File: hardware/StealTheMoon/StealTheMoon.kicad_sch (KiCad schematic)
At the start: 21 parts, among them J1 Motor, J2 Motor, J3 Servo, J4 Servo, J5 Conn_01x10, J6 BAT, U1 ESP32-DEVKIT-V1, U2 ROB-14450, U3 L7805CV, U4 L7805CV

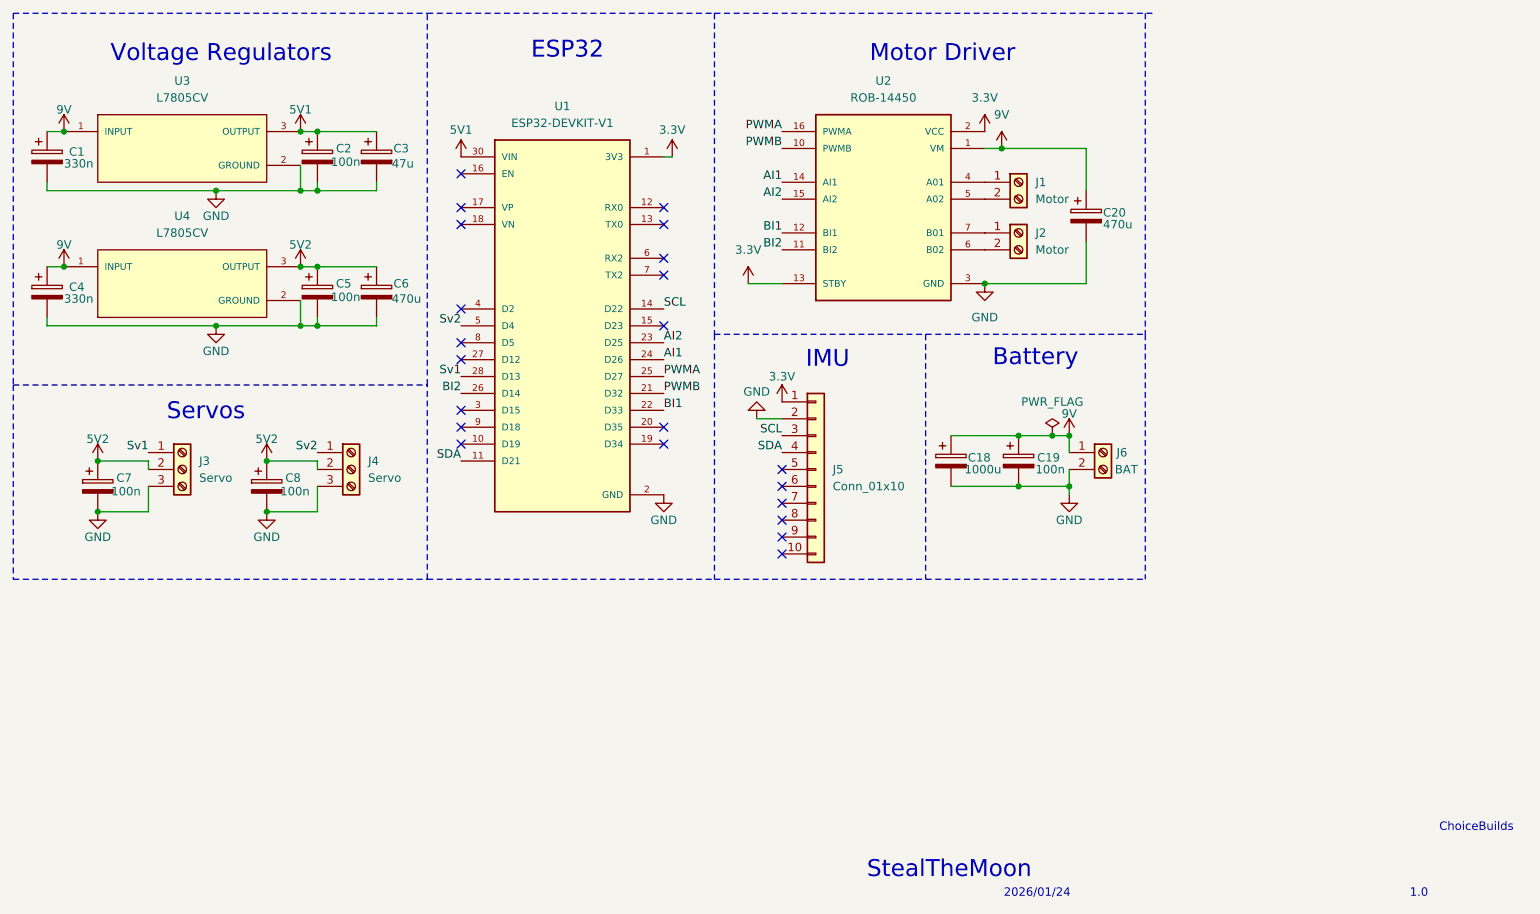
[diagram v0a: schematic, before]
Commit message: Finish layout and generate gbr files for fabrication
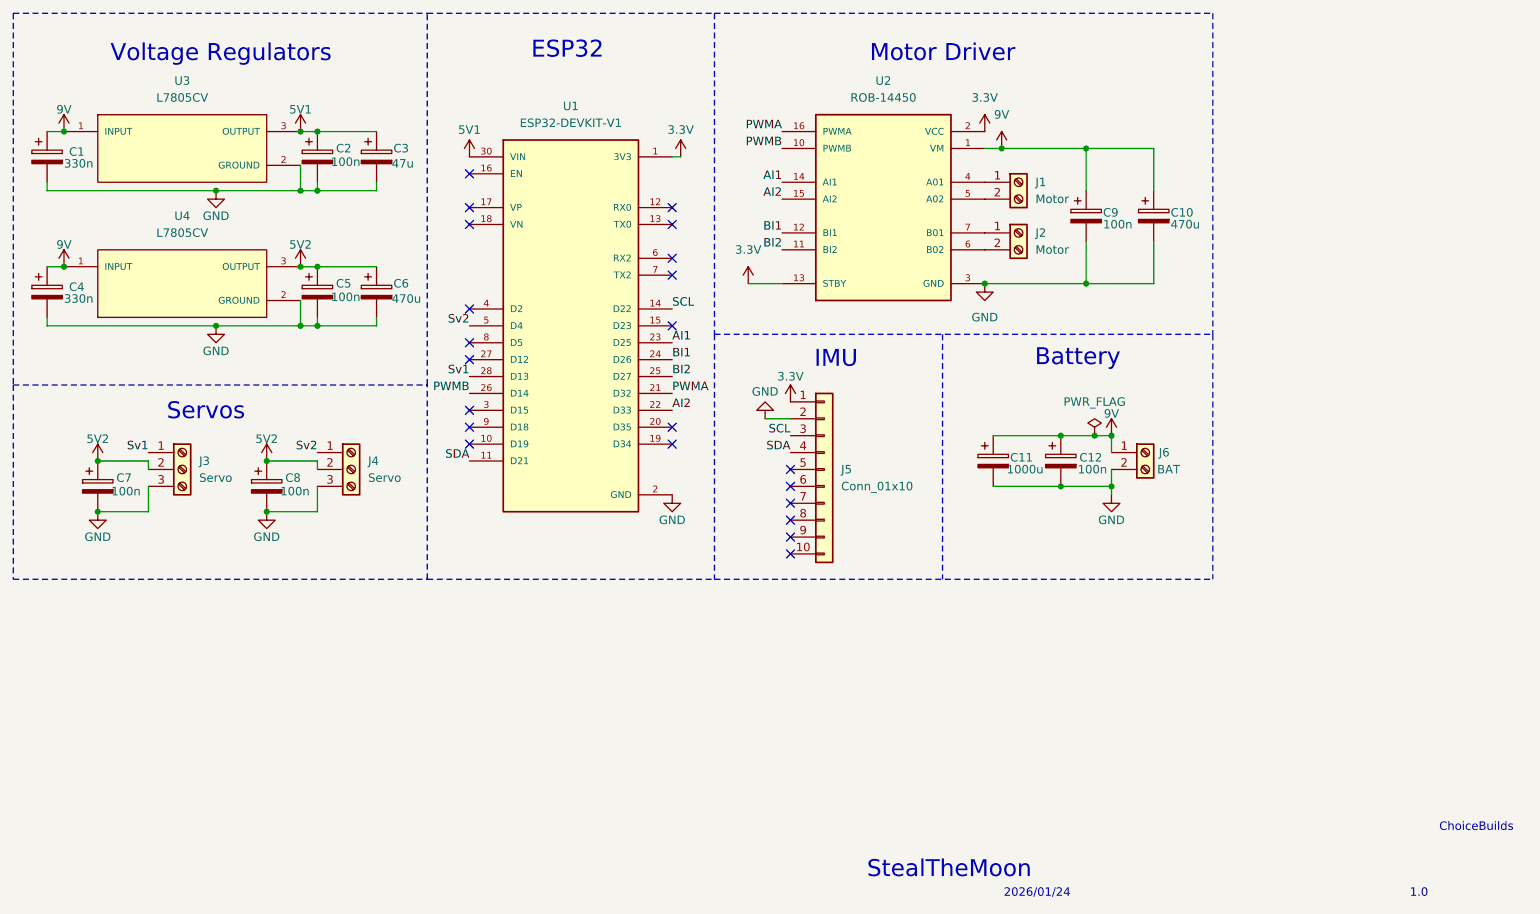
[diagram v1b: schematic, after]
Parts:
- added C9: 100n, Capacitor_THT:CP_Radial_D5.0mm_P2.50mm, symbol Device:C_Polarized
- renumbered C20 to C10, C18 to C11, C19 to C12
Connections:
- net 9V: now also C9.1
- net AI1: now also U1.23 (D25); no longer U1.24 (D26)
- net AI2: now also U1.22 (D33); no longer U1.23 (D25)
- net BI1: now also U1.24 (D26); no longer U1.22 (D33)
- net BI2: now also U1.25 (D27); no longer U1.26 (D14)
- net GND: now also C9.2
- net PWMA: now also U1.21 (D32); no longer U1.25 (D27)
- net PWMB: now also U1.26 (D14); no longer U1.21 (D32)
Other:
- moved on the sheet: C10, C11, C12, J5, J6, U1
